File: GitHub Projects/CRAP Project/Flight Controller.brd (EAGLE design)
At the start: 160 x 100 mm, 80 parts, among them J1 2POS_SCREWTERM, J2 4POS_SCREWTERM, J3 4POS_SCREWTERM, J4 4POS_SCREWTERM, Q101 IPD042P03L3G, Q102 IPD042P03L3G

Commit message: Added super cap part, did prelim board layout
1. Made a super capacitor part with a upright and folded variant.
2. Talked with Davis about the dimensions of the board and came to the
conclusion that 100mm tall will be alright.  Also speculated that 100mm
tall board would work with most club rockets, and confirmed with both
supersonic teams that 100mm tall would be able to fit.
3. Changed some of the modules in the upper level sheet to fit back on
the 0.1" grid, although some of the ports are still 0.05" off.
4. Renamed in the ordance sheet the long lines to PYRO+ and PYRO- to
allign with the module ports.
5. Attached PYRO+ and PYRO- in the top level sheet to the headers in the
same fashion each time
6. Named the nets of each firing circuit attachment to their
corresponding module and if they were + or -, e.g.: FC1+ or FC4-
7. On the silkscreen made + and - text on tPlace layer (top silkscreen
layer) and alligned with each firing pin.
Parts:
- added C305: (no value), CRAP Parts:AVX_1F_5V_FOLDED
- added J101: 2POS_SCREWTERM, CRAP Parts:2POS_0.1
- C104: value (none) -> 100n
- R103: value 470k, 1% -> 470k
- R104: value 150k, 1% -> 150k
- moved JP1 187.2 mm to (4.80, 41.1), turned to 90 degrees
- moved J4 171.6 mm to (34.0, 63.8), turned to 90 degrees
- moved J3 169.0 mm to (34.0, 53.6), turned to 90 degrees
- moved U1 159.8 mm to (20.0, 27.0), turned to 45 degrees
- moved J1 137.1 mm to (34.0, 71.4), turned to 270 degrees
- moved U$101 135.9 mm to (26.6, 47.7)
- moved J2 133.8 mm to (34.0, 84.1), turned to 90 degrees
- moved XB501 45.7 mm to (20.0, 15.5), turned to 180 degrees
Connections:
- net FIRING_CIRCUIT1:N$2 renamed FIRING_CIRCUIT1:PYRO-
- net FIRING_CIRCUIT2:N$2 renamed FIRING_CIRCUIT2:PYRO-
- net FIRING_CIRCUIT3:N$2 renamed FIRING_CIRCUIT3:PYRO-
- net FIRING_CIRCUIT4:N$2 renamed FIRING_CIRCUIT4:PYRO-
- removed net FIRING_CIRCUIT1:N$3: FIRING_CIRCUIT1:R1.1
- removed net FIRING_CIRCUIT2:N$3: FIRING_CIRCUIT2:R1.1
- removed net FIRING_CIRCUIT3:N$3: FIRING_CIRCUIT3:R1.1
- removed net FIRING_CIRCUIT4:N$3: FIRING_CIRCUIT4:R1.1
- removed net ORDNANCE_POWER:N$4: D301.1, D301.2
- removed net ORDNANCE_POWER:N$99: U301.P10
- new net FC1+: FIRING_CIRCUIT1:R1.1, J3.1
- new net FC1-: J3.2
- new net FC2+: FIRING_CIRCUIT2:R1.1, J3.3
- new net FC2-: J3.4
- new net FC3+: FIRING_CIRCUIT3:R1.1, J4.1
- new net FC3-: J4.2
- new net FC4+: FIRING_CIRCUIT4:R1.1, J4.3
- new net FC4-: J4.4
- new net ORDNANCE_POWER:N$3: C305.1, D301.1, D301.2, U301.P10
- net DCDC_REGULATOR:N$6: now also J101.2
- net GND: now also C305.2, J101.1
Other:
- board size 160 x 100 mm -> 40 x 90 mm
- board text added: "+"
- board text added: "-"

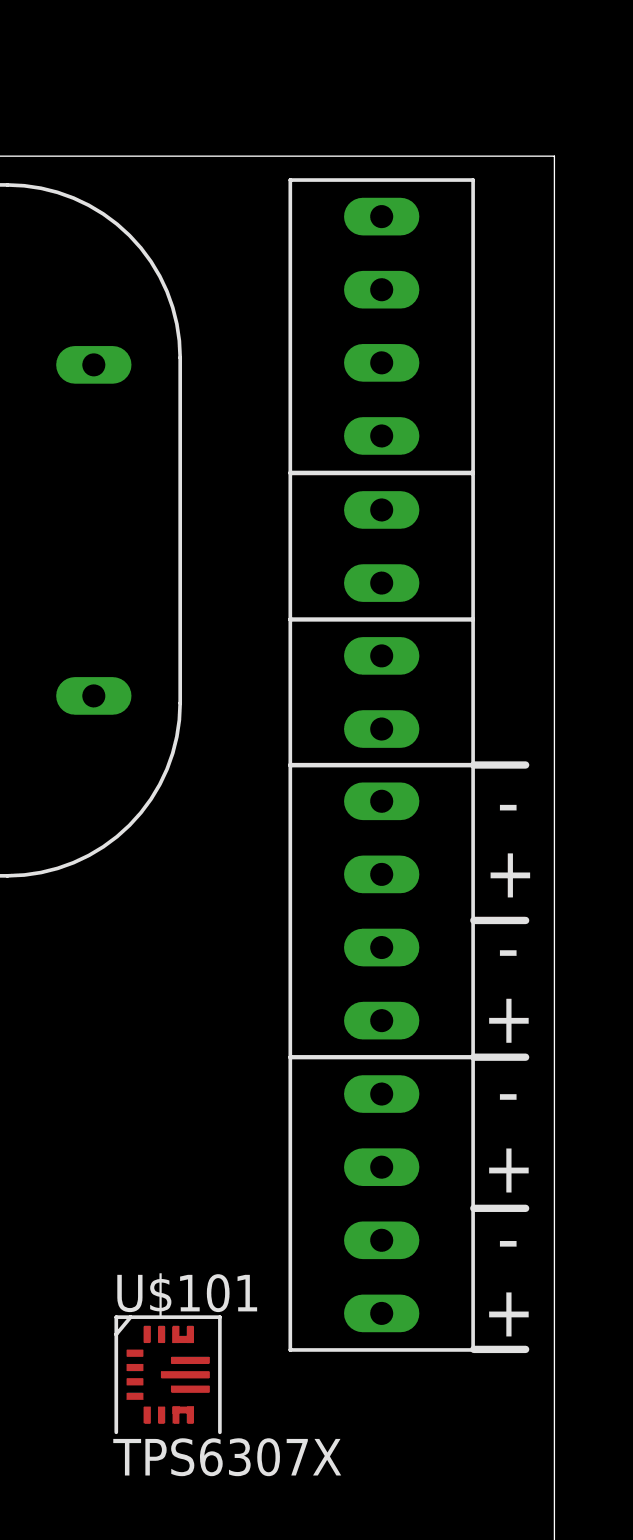
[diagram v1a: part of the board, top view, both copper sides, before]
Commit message: Changed silkscreen
1. Changed the silkscreen from numbers with + and - to what they were
going to be without + and -, because polarization doesn't matter when
dealing with a resistive component.
2. Also added the silkscreen names for the switch, temperature sensor,
and power input.
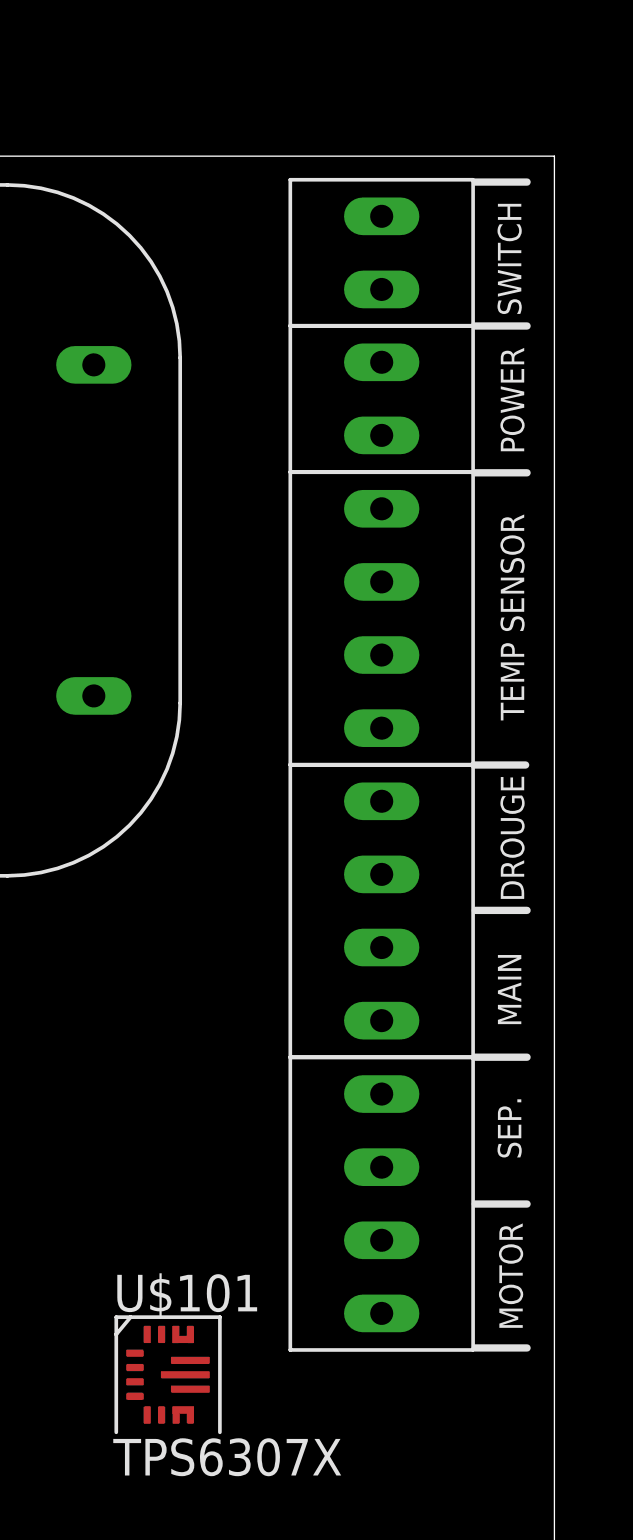
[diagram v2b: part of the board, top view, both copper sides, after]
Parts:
- moved J101 10.2 mm to (34.0, 86.6)
- moved J1 10.2 mm to (34.0, 81.6)
- moved J2 10.2 mm to (34.0, 73.9)
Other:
- board text added: "DROUGE"
- board text added: "MAIN"
- board text added: "MOTOR"
- board text added: "POWER"
- board text added: "SEP."
- board text added: "SWITCH"
- board text added: "TEMP SENSOR"
- board text removed: "+"
- board text removed: "-"
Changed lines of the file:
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@@
 <wire x1="40" y1="90" x2="0" y2="90" width="0" layer="20"/>
 <wire x1="0" y1="90" x2="0" y2="0" width="0" layer="20"/>
-<text x="37.5" y="49" size="1.778" layer="21">+</text>
-<text x="37.5" y="54" size="1.778" layer="21">+</text>
-<text x="37.5" y="59.2" size="1.778" layer="21">+</text>
-<text x="37.55" y="64.25" size="1.778" layer="21">+</text>
-<text x="38" y="66.7" size="1.778" layer="21">-</text>
-<text x="38" y="61.65" size="1.778" layer="21">-</text>
-<text x="38" y="56.65" size="1.778" layer="21">-</text>
-<text x="38" y="51.55" size="1.778" layer="21">-</text>
-<wire x1="37.2" y1="63.45" x2="39" y2="63.45" width="0.254" layer="21"/>
-<wire x1="37.2" y1="58.7" x2="39" y2="58.7" width="0.254" layer="21"/>
-<wire x1="37.2" y1="53.45" x2="39" y2="53.45" width="0.254" layer="21"/>
-<wire x1="37.2" y1="48.55" x2="39" y2="48.55" width="0.254" layer="21"/>
 <wire x1="37.2" y1="68.85" x2="39" y2="68.85" width="0.254" layer="21"/>
+<wire x1="37.25" y1="53.6" x2="39.05" y2="53.6" width="0.254" layer="21"/>
+<text x="38.9" y="49.2" size="0.8128" layer="21" rot="R90">MOTOR</text>
+<text x="38.85" y="55.15" size="0.8128" layer="21" rot="R90">SEP.</text>
+<text x="38.85" y="59.75" size="0.8128" layer="21" rot="R90">MAIN</text>
+<text x="38.95" y="64.1" size="0.8128" layer="21" rot="R90">DROUGE</text>
+<wire x1="37.25" y1="58.7" x2="39.05" y2="58.7" width="0.254" layer="21"/>
+<wire x1="37.25" y1="63.8" x2="39.05" y2="63.8" width="0.254" layer="21"/>
+<wire x1="37.25" y1="48.6" x2="39.05" y2="48.6" width="0.254" layer="21"/>
+<wire x1="37.25" y1="79" x2="39.05" y2="79" width="0.254" layer="21"/>
+<wire x1="37.25" y1="84.1" x2="39.05" y2="84.1" width="0.254" layer="21"/>
+<wire x1="37.25" y1="89.1" x2="39.05" y2="89.1" width="0.254" layer="21"/>
+<text x="38.95" y="70.4" size="0.8128" layer="21" rot="R90">TEMP SENSOR</text>
+<text x="38.95" y="79.65" size="0.8128" layer="21" rot="R90">POWER</text>
+<text x="38.85" y="84.45" size="0.8128" layer="21" rot="R90">SWITCH</text>
 </plain>
 <attributes>
@@
 <element name="FIRING_CIRCUIT4:U$1" library="transistor-power" package="SOT323" value="PMF170XP" x="-49.53" y="144.78"/>
 <element name="FIRING_CIRCUIT4:U$2" library="transistor-power" package="SO-08" value="DMG4800LSD" x="-17.78" y="125.73"/>
-<element name="J1" library="CRAP Parts" package="2POS_0.1" value="2POS_SCREWTERM" x="34" y="71.37" smashed="yes" rot="R270"/>
-<element name="J2" library="CRAP Parts" package="4POS_0.1" value="4POS_SCREWTERM" x="34" y="84.09" smashed="yes" rot="R90"/>
+<element name="J1" library="CRAP Parts" package="2POS_0.1" value="2POS_SCREWTERM" x="34" y="81.57" smashed="yes" rot="R270"/>
+<element name="J2" library="CRAP Parts" package="4POS_0.1" value="4POS_SCREWTERM" x="34" y="73.94" smashed="yes" rot="R90"/>
 <element name="J3" library="CRAP Parts" package="4POS_0.1" value="4POS_SCREWTERM" x="34" y="53.61" smashed="yes" rot="R90"/>
 <element name="J4" library="CRAP Parts" package="4POS_0.1" value="4POS_SCREWTERM" x="34" y="63.78" smashed="yes" rot="R90"/>
@@
 <element name="MEMORY1:U1" library="micron" package="SOP16" value="" x="-107.95" y="3.81"/>
 <element name="MEMORY1:C1" library="rcl" package="C0603" value="0.1u" x="-110.49" y="-7.62"/>
-<element name="J101" library="CRAP Parts" package="2POS_0.1" value="2POS_SCREWTERM" x="34" y="76.44" smashed="yes" rot="R90"/>
+<element name="J101" library="CRAP Parts" package="2POS_0.1" value="2POS_SCREWTERM" x="34" y="86.64" smashed="yes" rot="R90"/>
 <element name="C305" library="CRAP Parts" package="AVX_1F_5V_FOLDED" value="" x="24" y="77" rot="R90"/>
 </elements>
@@
 <wire x1="-19.02" y1="203.415" x2="-20.32" y2="205.74" width="0" layer="19" extent="1-1"/>
 <wire x1="-21.62" y1="203.415" x2="-19.02" y2="203.415" width="0" layer="19" extent="1-1"/>
-<wire x1="34" y1="70.1" x2="-21.62" y2="203.415" width="0" layer="19" extent="1-1"/>
-<wire x1="17.2776375" y1="32.197234375" x2="34" y2="70.1" width="0" layer="19" extent="1-1"/>
+<wire x1="34" y1="80.3" x2="-21.62" y2="203.415" width="0" layer="19" extent="1-1"/>
+<wire x1="17.2776375" y1="32.197234375" x2="34" y2="80.3" width="0" layer="19" extent="1-1"/>
 <wire x1="17.631190625" y1="21.449209375" x2="17.2776375" y2="32.197234375" width="0" layer="19" extent="1-1"/>
 <wire x1="25.5507875" y1="24.631190625" x2="17.631190625" y2="21.449209375" width="0" layer="19" extent="1-1"/>
@@
 <wire x1="-41.06" y1="2.54" x2="-47.41" y2="2.54" width="0" layer="19" extent="1-1"/>
 <wire x1="-96.39" y1="-1.54" x2="-79.59" y2="39.37" width="0" layer="19" extent="1-1"/>
-<wire x1="34" y1="75.17" x2="-96.39" y2="-1.54" width="0" layer="19" extent="1-1"/>
-<wire x1="24" y1="82.75" x2="34" y2="75.17" width="0" layer="19" extent="1-1"/>
+<wire x1="34" y1="85.37" x2="-96.39" y2="-1.54" width="0" layer="19" extent="1-1"/>
+<wire x1="24" y1="82.75" x2="34" y2="85.37" width="0" layer="19" extent="1-1"/>
 <wire x1="31" y1="24.5" x2="-17.145" y2="39.31" width="0" layer="19" extent="1-1"/>
 </signal>
@@
 <contactref element="J1" pad="1"/>
 <contactref element="Q101" pad="2"/>
-<wire x1="-16.77" y1="150.14" x2="34" y2="72.64" width="0" layer="19" extent="1-1"/>
+<wire x1="-16.77" y1="150.14" x2="34" y2="82.84" width="0" layer="19" extent="1-1"/>
 </signal>
 <signal name="VDDOUT">
@@
 <contactref element="J2" pad="1"/>
 <contactref element="U$401" pad="5"/>
-<wire x1="34" y1="80.28" x2="-22.645" y2="204.44" width="0" layer="19" extent="1-1"/>
+<wire x1="34" y1="70.13" x2="-22.645" y2="204.44" width="0" layer="19" extent="1-1"/>
 </signal>
 <signal name="N$7">
@@
 <contactref element="C403" pad="1"/>
 <wire x1="-28.79" y1="203.2" x2="-20.97" y2="203.415" width="0" layer="19" extent="1-1"/>
-<wire x1="34" y1="82.82" x2="-28.79" y2="203.2" width="0" layer="19" extent="1-1"/>
+<wire x1="34" y1="72.67" x2="-28.79" y2="203.2" width="0" layer="19" extent="1-1"/>
 </signal>
 <signal name="N$8">
@@
 <contactref element="C403" pad="2"/>
 <wire x1="-27.09" y1="203.2" x2="-20.32" y2="203.415" width="0" layer="19" extent="1-1"/>
-<wire x1="34" y1="85.36" x2="-27.09" y2="203.2" width="0" layer="19" extent="1-1"/>
+<wire x1="34" y1="75.21" x2="-27.09" y2="203.2" width="0" layer="19" extent="1-1"/>
 </signal>
 <signal name="N$9">
 <contactref element="J2" pad="4"/>
 <contactref element="U$401" pad="9"/>
-<wire x1="34" y1="87.9" x2="-19.67" y2="203.415" width="0" layer="19" extent="1-1"/>
+<wire x1="34" y1="77.75" x2="-19.67" y2="203.415" width="0" layer="19" extent="1-1"/>
 </signal>
 <signal name="MS5611_CS">
@@
 <contactref element="R102" pad="2"/>
 <contactref element="J101" pad="2"/>
-<wire x1="-86.78" y1="166.37" x2="34" y2="77.71" width="0" layer="19" extent="1-1"/>
+<wire x1="-86.78" y1="166.37" x2="34" y2="87.91" width="0" layer="19" extent="1-1"/>
 </signal>
 <signal name="FIRING_CIRCUIT1:N$1">

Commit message: IMU, Breakwire, Firing Chain module updates
1. Added CES521 diode to diode.lbr
2. Added CES521 to breakwire and pyro firing chain modules
3. Basic wiring of IMU module

Issues needing to be resolved with Evan
1. Address of IMU. There is a dangling resistor ready for this on the
top level schematic.
2. What does FSYNC need to be wired to inside the IMU module?
3. The breakwire and firing chain modules have two pins that I want
connected internally but named separately. See comments inside these
modules for more information.
4. What value of resistors to use for the IMU I2C lines. Currently 2.2k
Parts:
- added BREAKWIRE1:C1, BREAKWIRE2:C1, FIRING_CIRCUIT1:C1, FIRING_CIRCUIT2:C1, FIRING_CIRCUIT3:C1, FIRING_CIRCUIT4:C1, IMU1:C1, IMU1:C3: 0.1u, rcl:C0603
- added BREAKWIRE1:D1, BREAKWIRE2:D1, FIRING_CIRCUIT1:D1, FIRING_CIRCUIT2:D1, FIRING_CIRCUIT3:D1, FIRING_CIRCUIT4:D1: CES521SOD523, diode:SOD523
- added BREAKWIRE1:R1, BREAKWIRE2:R1, R1: 10k, rcl:R0603
- added FIRING_CIRCUIT1:R5, FIRING_CIRCUIT2:R5, FIRING_CIRCUIT3:R5, FIRING_CIRCUIT4:R5: 1M, rcl:R0603
- added IMU1:C2: 10n, rcl:C0603
- added IMU1:R2, IMU1:R3: 2.2K, rcl:R0603
- added J5: 4POS_SCREWTERM, CRAP Parts:4POS_0.1
- renumbered FIRING_CIRCUIT1:U$1 to FIRING_CIRCUIT1:Q1, FIRING_CIRCUIT1:U$2 to FIRING_CIRCUIT1:Q2, FIRING_CIRCUIT2:U$1 to FIRING_CIRCUIT2:Q1, FIRING_CIRCUIT2:U$2 to FIRING_CIRCUIT2:Q2, FIRING_CIRCUIT3:U$1 to FIRING_CIRCUIT3:Q1, FIRING_CIRCUIT3:U$2 to FIRING_CIRCUIT3:Q2, FIRING_CIRCUIT4:U$1 to FIRING_CIRCUIT4:Q1, FIRING_CIRCUIT4:U$2 to FIRING_CIRCUIT4:Q2
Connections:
- net FIRING_CIRCUIT1:N$7 renamed FIRING_CIRCUIT1:!CONT_EN
- net FIRING_CIRCUIT2:N$7 renamed FIRING_CIRCUIT2:!CONT_EN
- net FIRING_CIRCUIT3:N$7 renamed FIRING_CIRCUIT3:!CONT_EN
- net FIRING_CIRCUIT4:N$7 renamed FIRING_CIRCUIT4:!CONT_EN
- removed net FIRING_CIRCUIT1:N$6: FIRING_CIRCUIT1:Q1.1, FIRING_CIRCUIT1:R1.2
- removed net FIRING_CIRCUIT1:PYRO-: FIRING_CIRCUIT1:Q2.7, FIRING_CIRCUIT1:Q2.8
- removed net FIRING_CIRCUIT2:N$6: FIRING_CIRCUIT2:Q1.1, FIRING_CIRCUIT2:R1.2
- removed net FIRING_CIRCUIT2:PYRO-: FIRING_CIRCUIT2:Q2.7, FIRING_CIRCUIT2:Q2.8
- removed net FIRING_CIRCUIT3:N$6: FIRING_CIRCUIT3:Q1.1, FIRING_CIRCUIT3:R1.2
- removed net FIRING_CIRCUIT3:PYRO-: FIRING_CIRCUIT3:Q2.7, FIRING_CIRCUIT3:Q2.8
- removed net FIRING_CIRCUIT4:N$6: FIRING_CIRCUIT4:Q1.1, FIRING_CIRCUIT4:R1.2
- removed net FIRING_CIRCUIT4:PYRO-: FIRING_CIRCUIT4:Q2.7, FIRING_CIRCUIT4:Q2.8
- removed net IMU1:REGOUT: IMU1:U1.10
- removed net IMU1:RESV: IMU1:U1.1
- removed net IMU1:RESV/GND: IMU1:U1.20
- removed net IMU1:VDD: IMU1:U1.13
- new net BREAKWIRE1:N$1: BREAKWIRE1:D1.A, BREAKWIRE1:R1.1
- new net BREAKWIRE2:N$1: BREAKWIRE2:D1.A, BREAKWIRE2:R1.1
- new net FIRING_CIRCUIT1:N$2: FIRING_CIRCUIT1:D1.A, FIRING_CIRCUIT1:Q1.1
- new net FIRING_CIRCUIT1:N$3: FIRING_CIRCUIT1:D1.C, FIRING_CIRCUIT1:R1.2
- new net FIRING_CIRCUIT2:N$2: FIRING_CIRCUIT2:D1.A, FIRING_CIRCUIT2:Q1.1
- new net FIRING_CIRCUIT2:N$3: FIRING_CIRCUIT2:D1.C, FIRING_CIRCUIT2:R1.2
- new net FIRING_CIRCUIT3:N$2: FIRING_CIRCUIT3:D1.A, FIRING_CIRCUIT3:Q1.1
- new net FIRING_CIRCUIT3:N$3: FIRING_CIRCUIT3:D1.C, FIRING_CIRCUIT3:R1.2
- new net FIRING_CIRCUIT4:N$2: FIRING_CIRCUIT4:D1.A, FIRING_CIRCUIT4:Q1.1
- new net FIRING_CIRCUIT4:N$3: FIRING_CIRCUIT4:D1.C, FIRING_CIRCUIT4:R1.2
- new net IMU1:+3V3: IMU1:C1.1, IMU1:C2.1, IMU1:U1.1, IMU1:U1.10, IMU1:U1.8
- new net IMU1:AD0: IMU1:U1.9
- new net IMU1:INT: IMU1:U1.12
- new net IMU1:SCL: IMU1:R2.1, IMU1:U1.23
- new net IMU1:SDA: IMU1:R3.1, IMU1:U1.24
- new net N$10: BREAKWIRE1:C1.1, J5.2
- new net N$11: BREAKWIRE2:D1.C, J5.3
- new net N$12: BREAKWIRE2:C1.1, J5.4
- new net N$13: BREAKWIRE1:D1.C, J5.1
- net +3V3: now also BREAKWIRE1:R1.2, BREAKWIRE2:R1.2, IMU1:C3.1, IMU1:R2.2, IMU1:R3.2, IMU1:U1.13, IMU1:U1.22; no longer IMU1:U1.8
- net FC1+: now also FIRING_CIRCUIT1:R5.2
- net FC1-: now also FIRING_CIRCUIT1:C1.1, FIRING_CIRCUIT1:Q2.7, FIRING_CIRCUIT1:Q2.8, FIRING_CIRCUIT1:R5.1
- net FC2+: now also FIRING_CIRCUIT2:R5.2
- net FC2-: now also FIRING_CIRCUIT2:C1.1, FIRING_CIRCUIT2:Q2.7, FIRING_CIRCUIT2:Q2.8, FIRING_CIRCUIT2:R5.1
- net FC3+: now also FIRING_CIRCUIT3:R5.2
- net FC3-: now also FIRING_CIRCUIT3:C1.1, FIRING_CIRCUIT3:Q2.7, FIRING_CIRCUIT3:Q2.8, FIRING_CIRCUIT3:R5.1
- net FC4+: now also FIRING_CIRCUIT4:R5.2
- net FC4-: now also FIRING_CIRCUIT4:C1.1, FIRING_CIRCUIT4:Q2.7, FIRING_CIRCUIT4:Q2.8, FIRING_CIRCUIT4:R5.1
- net GND: now also BREAKWIRE1:C1.2, BREAKWIRE2:C1.2, FIRING_CIRCUIT1:C1.2, FIRING_CIRCUIT2:C1.2, FIRING_CIRCUIT3:C1.2, FIRING_CIRCUIT4:C1.2, IMU1:C1.2, IMU1:C2.2, IMU1:C3.2, IMU1:U1.20
